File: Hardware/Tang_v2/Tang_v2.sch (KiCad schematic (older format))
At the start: 2 parts

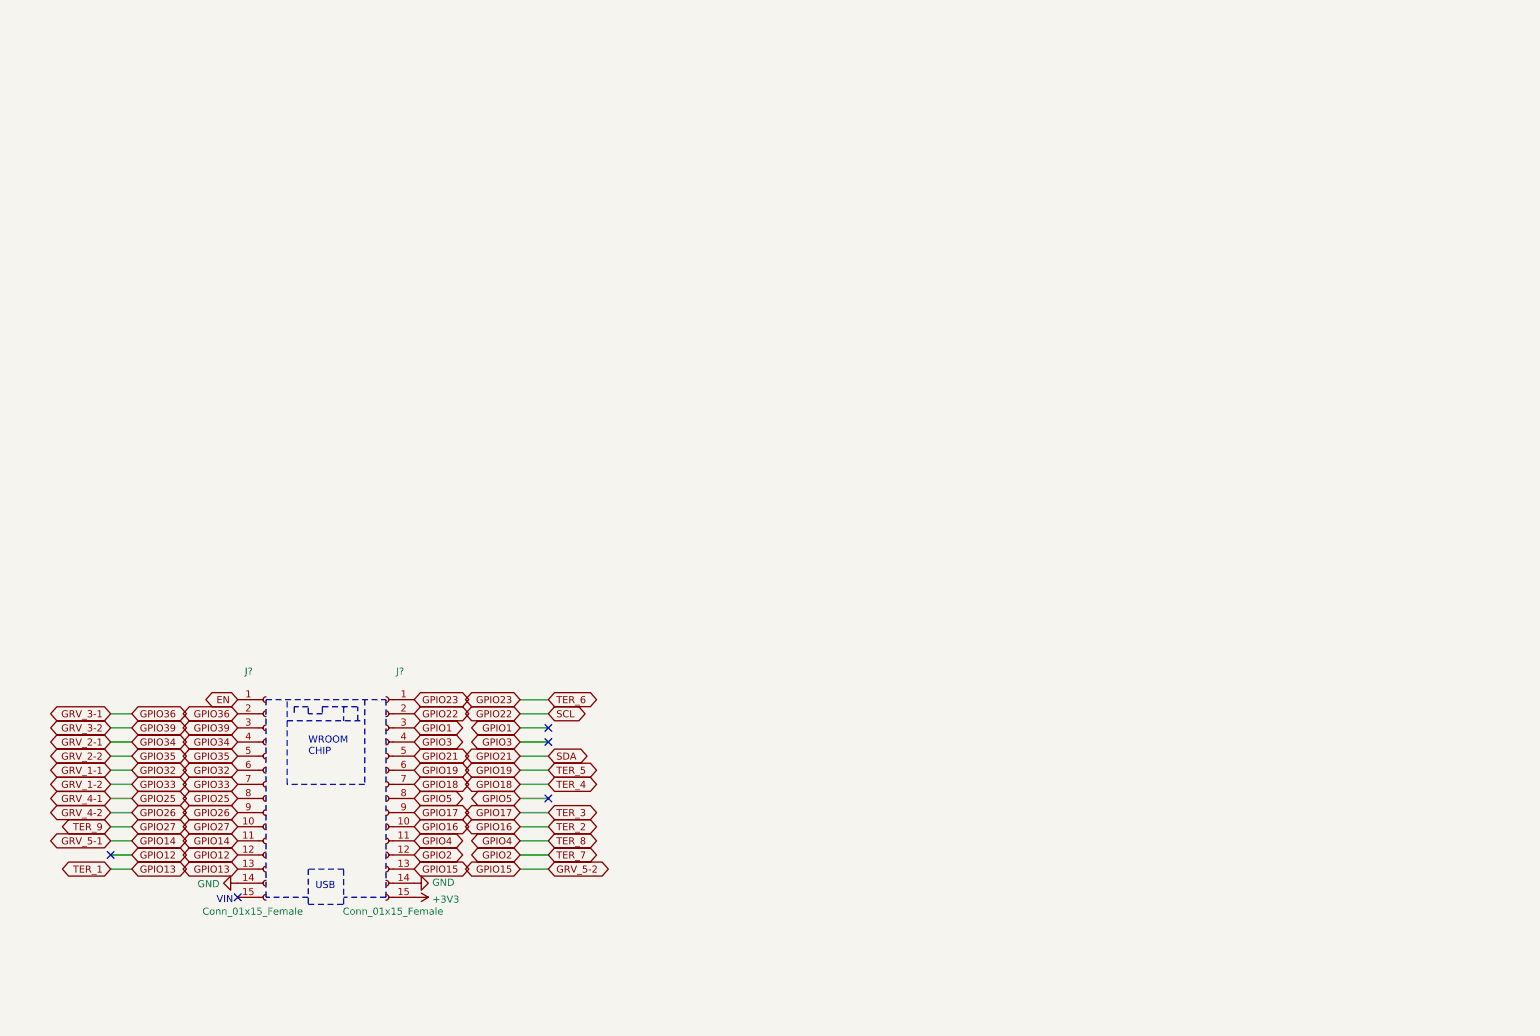
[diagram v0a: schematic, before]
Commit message: Added power switches
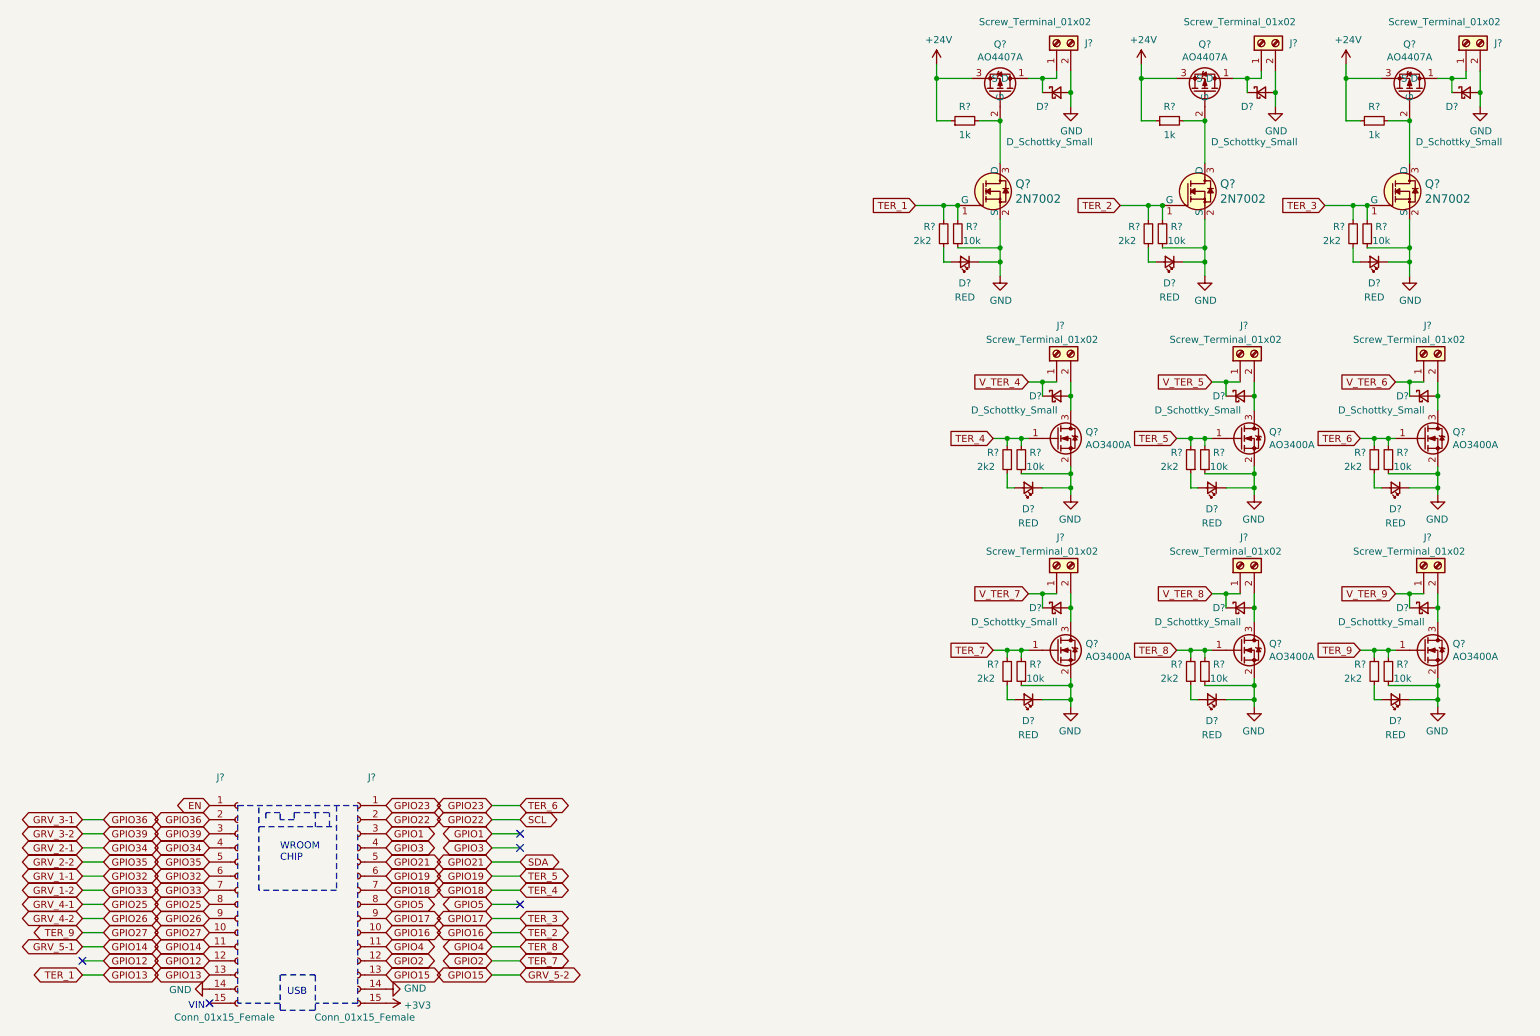
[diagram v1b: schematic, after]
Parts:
- added D? (x9): D_Schottky_Small, symbol Device:D_Schottky_Small
- added D? (x9): RED, symbol Device:LED_Small
- added J? (x9): Screw_Terminal_01x02, symbol Connector:Screw_Terminal_01x02
- added Q? (x3): AO4407A, symbol RasmusKiCadLibrary:AO4407A
- added Q? (x3): 2N7002, digikey-footprints:SOT-23-3, symbol dk_Transistors-FETs-MOSFETs-Single:2N7002
- added Q? (x6): AO3400A, Package_TO_SOT_SMD:SOT-23, symbol Transistor_FET:AO3400A
- added R? (x3): 1k, symbol Device:R_Small
- added R? (x9): 10k, symbol Device:R_Small
- added R? (x9): 2k2, symbol Device:R_Small
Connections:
- net GND: now also D?.1 (K), D?.1 (K), D?.1 (K), D?.1 (K), D?.1 (K), D?.1 (K), D?.1 (K), D?.1 (K), D?.1 (K), D?.2 (A), D?.2 (A), D?.2 (A), J?.2 (Pin_2), J?.2 (Pin_2), J?.2 (Pin_2), Q?.2 (S), Q?.2 (S), Q?.2 (S), Q?.2 (S), Q?.2 (S), Q?.2 (S), Q?.2 (S), Q?.2 (S), Q?.2 (S), R?.1, R?.1, R?.1, R?.1, R?.1, R?.1, R?.1, R?.1, R?.1
- net GPIO13: now also Q?.1 (G), R?.2, R?.2
- net GPIO16: now also Q?.1 (G), R?.2, R?.2
- net GPIO17: now also Q?.1 (G), R?.2, R?.2
- net GPIO18: now also Q?.1 (G), R?.2, R?.2
- net GPIO19: now also Q?.1 (G), R?.2, R?.2
- net GPIO2: now also Q?.1 (G), R?.2, R?.2
- net GPIO23: now also Q?.1 (G), R?.2, R?.2
- net GPIO27: now also Q?.1 (G), R?.2, R?.2
- net GPIO4: now also Q?.1 (G), R?.2, R?.2
- new net: D?.1 (K), J?.1 (Pin_1), Q?.1 (D) (x3)
- new net: Q?.2 (G), Q?.3 (D), R?.2 (x3)
- new net: D?.2 (A), R?.1 (x9)
- new net: D?.2 (A), J?.2 (Pin_2), Q?.3 (D) (x6)
- new net +24V: Q?.3 (S), Q?.3 (S), Q?.3 (S), R?.1, R?.1, R?.1
- new net V_TER_4: D?.1 (K), J?.1 (Pin_1)
- new net V_TER_5: D?.1 (K), J?.1 (Pin_1)
- new net V_TER_6: D?.1 (K), J?.1 (Pin_1)
- new net V_TER_7: D?.1 (K), J?.1 (Pin_1)
- new net V_TER_8: D?.1 (K), J?.1 (Pin_1)
- new net V_TER_9: D?.1 (K), J?.1 (Pin_1)
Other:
- moved on the sheet: J?

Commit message: Added v1.1 and v2 WIP
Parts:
- added C?: 100n, symbol Device:C_Small
- added C? (x2): CP1_Small, symbol Device:CP1_Small
- added C?: 50u, symbol Device:C_Small
- added C?: 1n, symbol Device:C_Small
- added D? (x2): D_Schottky_Small, symbol Device:D_Schottky_Small
- added F?: 20A, symbol Device:Fuse_Small
- added J?: Jack-DC, symbol Connector:Jack-DC
- added L?: L_Small, symbol Device:L_Small
- added Q?: no fucking clue yet, Package_TO_SOT_SMD:SOT-23, symbol Transistor_FET:AO3400A
- added R?: 5k, symbol Device:R_Small
- added R?: 3R, symbol Device:R_Small
- added R?: help me, symbol Device:R_Small
- added U?: UC3843_SOIC8, Package_SO:SOIC-8_3.9x4.9mm_P1.27mm, symbol Regulator_Controller:UC3843_SOIC8
- R? (x3): value 1k -> 10k
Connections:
- net +24V: now also C?.1, C?.2, C?.2, D?.1 (K), Q?.3 (D), U?.7 (VCC)
- net GND: now also C?.1, C?.1, C?.1, C?.2, C?.2, D?.2 (A), J?.2, R?.2, U?.5 (GND)
- new net: F?.1, J?.1
- new net: D?.2 (A), F?.2
- new net: R?.1, U?.3 (CS)
- new net: C?.2, R?.2, U?.4 (RC)
- new net: R?.2, U?.6 (OUT)
- new net: R?.1, U?.8 (VREF)
- new net: Q?.1 (G), R?.1
- new net: D?.1 (K), L?.1, Q?.2 (S)
- new net +12V: C?.1, L?.2
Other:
- note added: "5k and 1n should give\napproximately 300 kHz\nswitching frequency"
- note added: "THIS ALL HAS TO BE CHANGED TO ANOTHER CHIP\nFOR EXAMPLE: LM3485"
